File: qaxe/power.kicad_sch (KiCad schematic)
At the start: 76 parts, among them Q3 CSD16415Q5T, Q4 CSD16415Q5T, Q7 CSD16415Q5T, Q8 CSD16415Q5T, U17 LTC3856, U3 AP3211, U36 NCP1117ST33, U4 +0V8, U5 MCP1824T-1802E, U6 MCP1824T-0802E

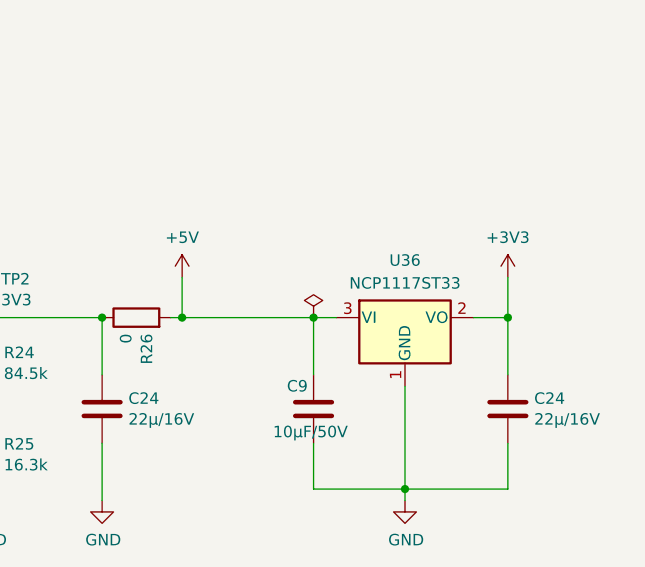
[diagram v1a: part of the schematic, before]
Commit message: updated BOM and replaces bss138 and 3.3V LDO with parts that are available
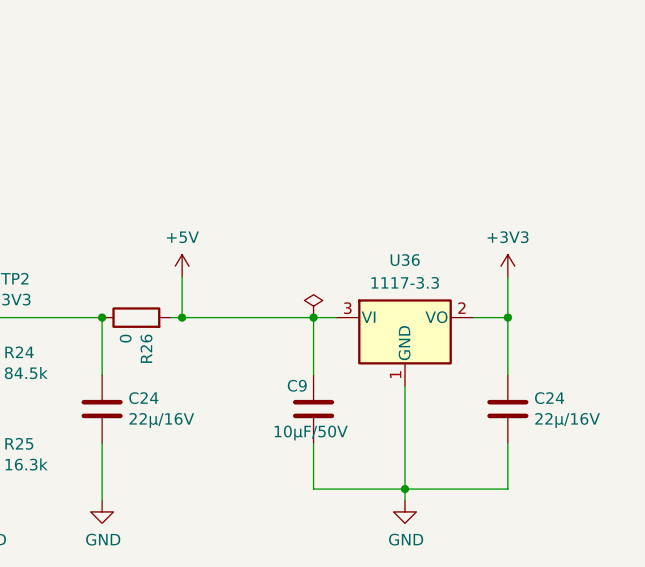
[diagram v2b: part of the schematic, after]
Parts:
- U36: value NCP1117ST33 -> 1117-3.3; Distributor (none) -> D; Manufacturer (none) -> LM1117IMPX-ADJNOPB; OrderNr (none) -> 488-LM1117IMPX-ADJNOPBCT-ND
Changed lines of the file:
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@@
       (effects (font (size 1.27 1.27)))
     )
-    (property "Value" "NCP1117ST33" (at 378.46 162.56 0)
+    (property "Value" "1117-3.3" (at 378.46 162.56 0)
       (effects (font (size 1.27 1.27)))
     )
@@
       (effects (font (size 1.27 1.27)) hide)
     )
-    (property "Distributor" "" (at 378.46 166.37 0)
+    (property "Distributor" "D" (at 378.46 166.37 0)
       (effects (font (size 1.27 1.27)) hide)
     )
+    (property "Manufacturer" "LM1117IMPX-ADJNOPB" (at 378.46 166.37 0)
+      (effects (font (size 1.27 1.27)) hide)
+    )
+    (property "OrderNr" "488-LM1117IMPX-ADJNOPBCT-ND" (at 378.46 166.37 0)
+      (effects (font (size 1.27 1.27)) hide)
+    )

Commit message: rev3
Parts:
- removed C56, C58, C59: 100µ/6.3V, Capacitor_SMD:C_1210_3225Metric, symbol Device:C
- removed NT1 (x2): NetTie_2, NetTie:NetTie-2_SMD_Pad0.5mm, symbol Device:NetTie_2
- added C39, C45, C48: 330µ/6.3V, Capacitor_Tantalum_SMD:CP_EIA-7343-15_Kemet-W, symbol Device:C_Polarized
- C55: value 100µ/6.3V -> 4.7µ/6.3V; footprint Capacitor_SMD:C_1210_3225Metric -> Capacitor_SMD:C_1206_3216Metric; Manufacturer C1210C107M9PAC7800 -> (none); OrderNr 399-C1210C107M9PAC7800CT-ND -> (none)
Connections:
- net +1V2: now also R24.1, C39.1, C45.1, C48.1
- net GND: now also R16.1, C39.2, C45.2, C48.2

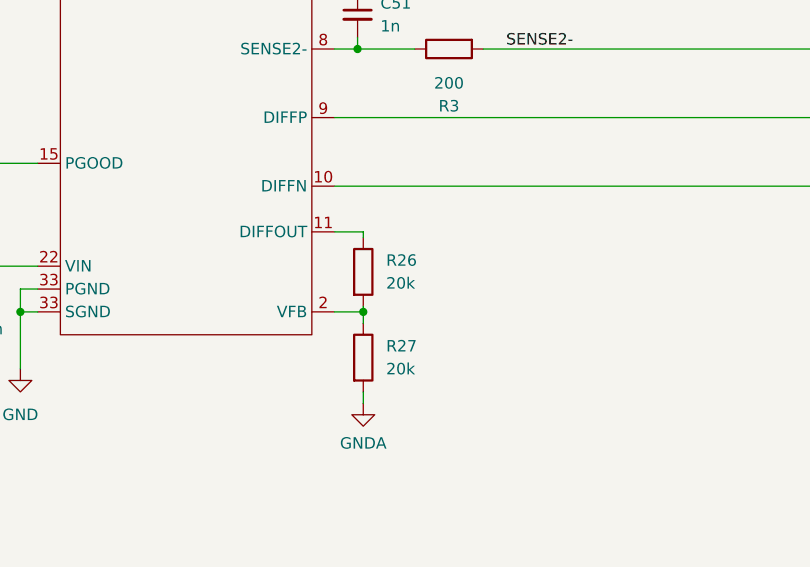
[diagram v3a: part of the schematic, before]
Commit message: replaced 20k with 22k on feedback voltage divider to increase core voltage by 0.05V. 485MHz working properly now at 100% cooling
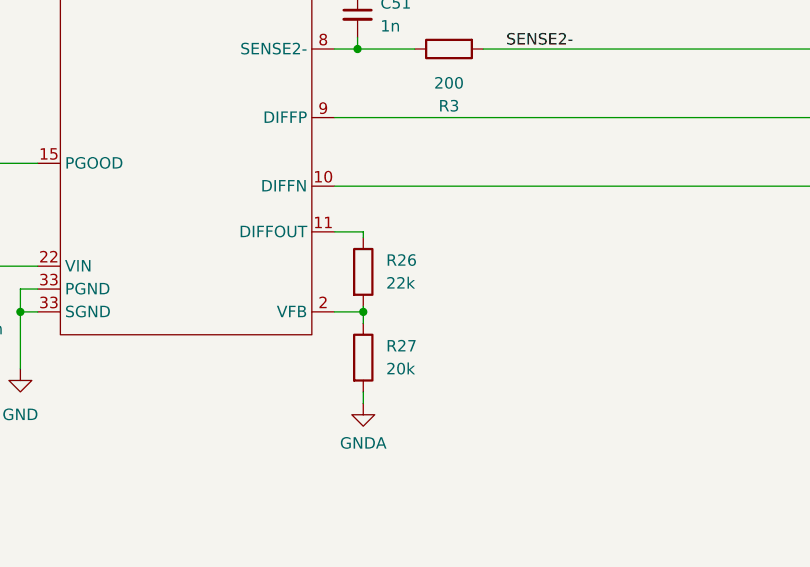
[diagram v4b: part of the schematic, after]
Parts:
- R26: value 20k -> 22k
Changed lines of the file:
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@@
       (effects (font (size 1.27 1.27)) (justify left))
     )
-    (property "Value" "20k" (at 142.24 198.12 0)
+    (property "Value" "22k" (at 142.24 198.12 0)
       (effects (font (size 1.27 1.27)) (justify left))
     )

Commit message: 4.7u cap was missing in digikey bom
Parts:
- C55: Distributor D -> (none)
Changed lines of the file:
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@@
       (effects (font (size 1.27 1.27)) hide)
     )
-    (property "Distributor" "D" (at 278.765 109.855 0)
+    (property "Distributor" "" (at 278.765 109.855 0)
       (effects (font (size 1.27 1.27)) hide)
     )
